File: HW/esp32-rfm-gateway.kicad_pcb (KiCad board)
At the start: 2 copper layers, 99 x 93.5 mm, 89 parts, among them J1 ph_1x2, J2 ph_1x2, J20 220V~, J21 ph_1x2, J22 s14500, J23 s18650, J24 ph_1x3, J25 ph_1x2, J3 ph_1x3, J30 AntSMA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

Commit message: Adds a new I2C connector, a LED for 5V indication, some SMD connections for a few free pins and labels
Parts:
- added D29: LEDG, CalinGeneric:LED0805HS, F.Cu at (112.5, 125.2)
- added J10: CS_1, CalinConnectors:SMD_Pins_1x1, F.Cu at (114.5, 57.9)
- added J11: CS_1, CalinConnectors:SMD_Pins_1x1, F.Cu at (114.5, 59.9)
- added J12: CS_1, CalinConnectors:SMD_Pins_1x1, F.Cu at (114.5, 61.9)
- added J13: CS_1, CalinConnectors:SMD_Pins_1x1, F.Cu at (114.5, 63.9)
- added J14: CS_1, CalinConnectors:SMD_Pins_1x1, F.Cu at (114.5, 65.9)
- added J8: ph_1x4, CalinConnectors:Pin_Header_Straight_1x04, F.Cu at (118.2, 103.5)
- added R29: 330, CalinGeneric:R0805HS, F.Cu at (112.5, 128.2)
- D20: value LEDchg -> LEDG
- moved SYM2 3.50 mm to (106.8, 134.0)
- moved J21 1.54 mm to (106.8, 125.5)
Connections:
- U1 pad 26: (no net) -> /IO4
- U1 pad 29: (no net) -> /IO5
- U1 pad 30: (no net) -> /IO18
- U1 pad 31: (no net) -> /IO19
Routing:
- net +5VP: track 72.1 -> 86.6 mm
- net /IO4: track 0.00 -> 5.63 mm
- net /IO19: track 0.00 -> 5.55 mm
- net /IO5: track 0.00 -> 5.55 mm
- net /IO18: track 0.00 -> 5.25 mm
- net Net-(D29-PadK): track 0.00 -> 3.00 mm
- net +3V3: track 299.6 -> 302.1 mm
- net /U0RXD: track 31.8 -> 30.3 mm
- net GND: track 925.0 -> 926.0 mm, vias 56 -> 54
- net /U0TXD: track 31.2 -> 30.2 mm
- net /SDA: track 117.6 -> 118.1 mm
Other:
- board text added: "+5V"
- board text added: "B"
- board text added: "DTR RTS"
- board text added: "SCL SDA"
- board text added: "SDA SCL"
- board text added: "Tx Rx"
- board text added: "designed with KiCad for hand soldering"
- board text added: "github.com CalinRadoni esp32-rfm-gateway"
- board text added: "rev.32"
- board text removed: "rev.30"

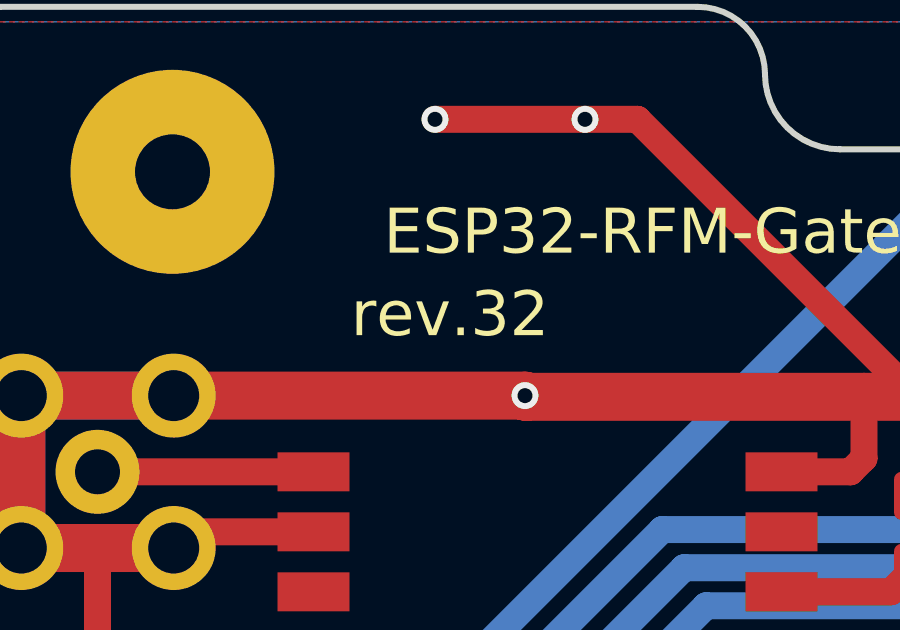
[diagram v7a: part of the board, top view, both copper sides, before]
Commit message: Updates components to add manufacturer, part number, ... fields. Also checked some values.
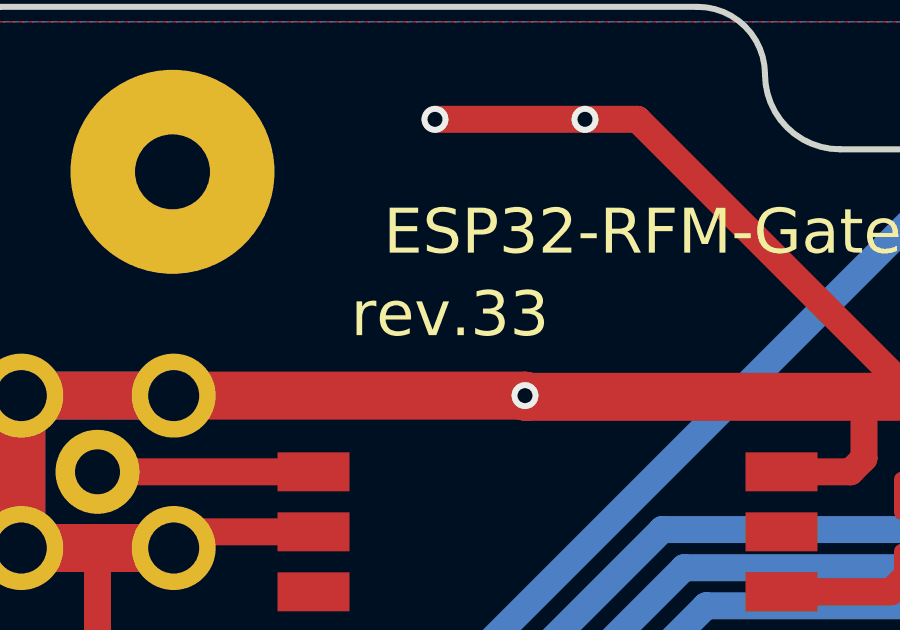
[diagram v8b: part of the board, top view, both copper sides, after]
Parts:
- C11: value 1uF -> 4,7uF
- C23: value 10uF -> 10uF/10V/1mOhm
- C24: value 22uF/1mOhm -> 22uF/6.3V/1mOhm
- D20: value LEDG -> LED-DNP
- D29: value LEDG -> LED Green
- R20: value 2K2 -> 2k2
- R21: value 330 -> 330-DNP
- R40, R41: value 10K -> 10k
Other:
- board text added: "rev.33"
- board text removed: "rev.32"
